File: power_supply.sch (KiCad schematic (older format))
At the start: 0 parts

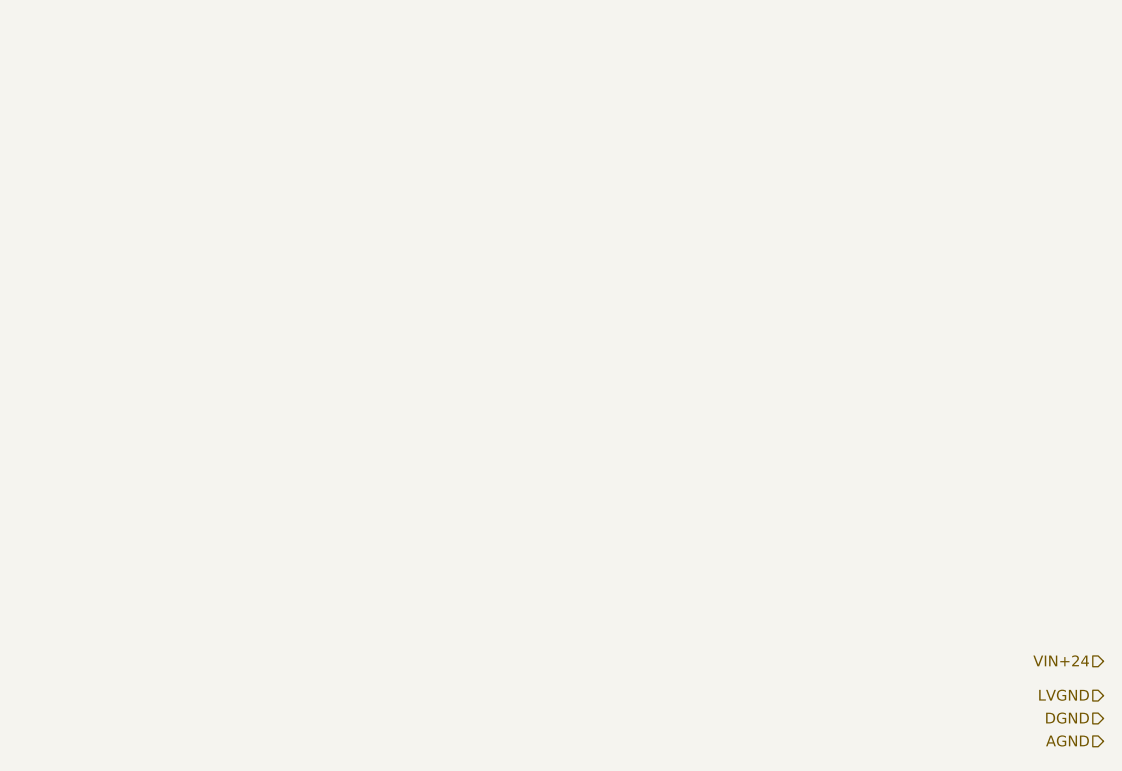
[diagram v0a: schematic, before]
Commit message: added some ICs, started on power, changed sheet sizes
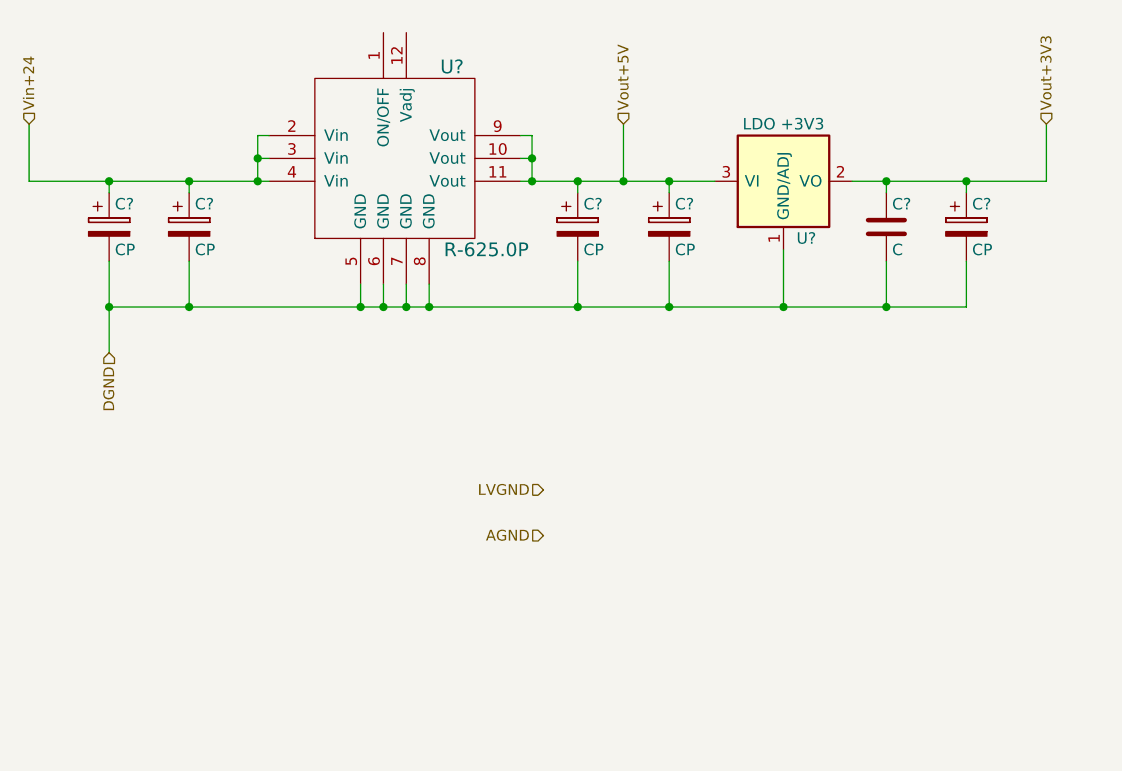
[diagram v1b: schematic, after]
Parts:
- added C? (x5): CP, symbol CP
- added C?: C, symbol C
- added U?: R-625.0P, symbol R-625.0P
- added U?: LDO +3V3, TO_SOT_Packages_SMD:SOT-223, symbol AP1117
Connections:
- net DGND: now also C?.2, C?.2, C?.2, C?.2, C?.2, C?.2, U?.1 (GND/ADJ), U?.5 (GND), U?.6 (GND), U?.7 (GND), U?.8 (GND)
- new net Vin+24: C?.1, C?.1, U?.2 (Vin), U?.3 (Vin), U?.4 (Vin)
- new net Vout+3V3: C?.1, C?.1, U?.2 (VO)
- new net Vout+5V: C?.1, C?.1, U?.10 (Vout), U?.11 (Vout), U?.3 (VI), U?.9 (Vout)
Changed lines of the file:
@@
 EELAYER 25 0
 EELAYER END
-$Descr A4 11693 8268
+$Descr User 7874 5906
 encoding utf-8
 Sheet 10 12
@@
 Comment4 ""
 $EndDescr
-Text HLabel 6050 4700 0    47   Input ~ 0
+Text HLabel 1700 3100 3    47   Input ~ 0
 DGND
-Text HLabel 6050 4800 0    47   Input ~ 0
+Text HLabel 3600 3900 0    47   Input ~ 0
 AGND
-Text HLabel 6050 4450 0    47   Input ~ 0
-VIN+24
-Text HLabel 6050 4600 0    47   Input ~ 0
+Text HLabel 1350 2100 1    47   Input ~ 0
+Vin+24
+Text HLabel 3600 3700 0    47   Input ~ 0
 LVGND
+$Comp
+L CP C?
+U 1 1 572CCDDB
+P 1700 2550
+F 0 "C?" H 1725 2650 50  0000 L CNN
+F 1 "CP" H 1725 2450 50  0000 L CNN
+F 2 "" H 1738 2400 50  0000 C CNN
+F 3 "" H 1700 2550 50  0000 C CNN
+	1    1700 2550
+	1    0    0    -1
+$EndComp
+$Comp
+L CP C?
+U 1 1 572CCE58
+P 2050 2550
+F 0 "C?" H 2075 2650 50  0000 L CNN
+F 1 "CP" H 2075 2450 50  0000 L CNN
+F 2 "" H 2088 2400 50  0000 C CNN
+F 3 "" H 2050 2550 50  0000 C CNN
+	1    2050 2550
+	1    0    0    -1
+$EndComp
+$Comp
+L CP C?
+U 1 1 572CCE73
+P 3750 2550
+F 0 "C?" H 3775 2650 50  0000 L CNN
+F 1 "CP" H 3775 2450 50  0000 L CNN
+F 2 "" H 3788 2400 50  0000 C CNN
+F 3 "" H 3750 2550 50  0000 C CNN
+	1    3750 2550
+	1    0    0    -1
+$EndComp
+$Comp
+L CP C?
+U 1 1 572CCEA6
+P 4150 2550
+F 0 "C?" H 4175 2650 50  0000 L CNN
+F 1 "CP" H 4175 2450 50  0000 L CNN
+F 2 "" H 4188 2400 50  0000 C CNN
+F 3 "" H 4150 2550 50  0000 C CNN
+	1    4150 2550
+	1    0    0    -1
+$EndComp
+$Comp
+L AP1117 U?
+U 1 1 572CD269
+P 4650 2350
+F 0 "U?" H 4750 2100 50  0000 C CNN
+F 1 "LDO +3V3" H 4650 2600 50  0000 C CNN
+F 2 "TO_SOT_Packages_SMD:SOT-223" H 4650 2350 50  0001 C CNN
+F 3 "" H 4650 2350 50  0000 C CNN
+	1    4650 2350
+	1    0    0    -1
+$EndComp
+$Comp
+L CP C?
+U 1 1 572CD599
+P 5450 2550
+F 0 "C?" H 5475 2650 50  0000 L CNN
+F 1 "CP" H 5475 2450 50  0000 L CNN
+F 2 "" H 5488 2400 50  0000 C CNN
+F 3 "" H 5450 2550 50  0000 C CNN
+	1    5450 2550
+	1    0    0    -1
+$EndComp
+$Comp
+L C C?
+U 1 1 572CD71C
+P 5100 2550
+F 0 "C?" H 5125 2650 50  0000 L CNN
+F 1 "C" H 5125 2450 50  0000 L CNN
+F 2 "" H 5138 2400 50  0000 C CNN
+F 3 "" H 5100 2550 50  0000 C CNN
+	1    5100 2550
+	1    0    0    -1
+$EndComp
+Wire Wire Line
+	4950 2350 5800 2350
+Wire Wire Line
+	5800 2350 5800 2100
+Wire Wire Line
+	5450 2400 5450 2350
+Connection ~ 5450 2350
+Wire Wire Line
+	5100 2400 5100 2350
+Connection ~ 5100 2350
+Wire Wire Line
+	3500 2350 4350 2350
+Wire Wire Line
+	3750 2400 3750 2350
+Wire Wire Line
+	4150 2400 4150 2350
+Connection ~ 4150 2350
+Text HLabel 5800 2100 1    47   Input ~ 0
+Vout+3V3
+Connection ~ 3750 2350
+Wire Wire Line
+	3950 2350 3950 2100
+Connection ~ 3950 2350
+Text HLabel 3950 2100 1    47   Input ~ 0
+Vout+5V
+Wire Wire Line
+	1350 2350 1350 2100
+Wire Wire Line
+	1700 2400 1700 2350
+Connection ~ 1700 2350
+Wire Wire Line
+	2050 2400 2050 2350
+Connection ~ 2050 2350
+$Comp
+L R-625.0P U?
+U 1 1 5729C579
+P 2600 2600
+F 0 "U?" H 3200 3350 60  0000 C CNN
+F 1 "R-625.0P" H 3350 2550 60  0000 C CNN
+F 2 "" H 2600 2600 60  0000 C CNN
+F 3 "" H 2600 2600 60  0000 C CNN
+	1    2600 2600
+	1    0    0    -1
+$EndComp
+Wire Wire Line
+	3500 2150 3550 2150
+Wire Wire Line
+	3550 2150 3550 2350
+Connection ~ 3550 2350
+Wire Wire Line
+	3500 2250 3550 2250
+Connection ~ 3550 2250
+Wire Wire Line
+	2400 2350 1350 2350
+Wire Wire Line
+	2400 2250 2350 2250
+Wire Wire Line
+	2350 2150 2350 2350
+Connection ~ 2350 2350
+Wire Wire Line
+	2400 2150 2350 2150
+Connection ~ 2350 2250
+Wire Wire Line
+	5450 2700 5450 2900
+Wire Wire Line
+	5450 2900 1700 2900
+Wire Wire Line
+	1700 2700 1700 3100
+Connection ~ 1700 2900
+Wire Wire Line
+	2800 2800 2800 2900
+Connection ~ 2800 2900
+Wire Wire Line
+	2900 2800 2900 2900
+Connection ~ 2900 2900
+Wire Wire Line
+	3000 2800 3000 2900
+Connection ~ 3000 2900
+Wire Wire Line
+	3100 2800 3100 2900
+Connection ~ 3100 2900
+Wire Wire Line
+	2050 2700 2050 2900
+Connection ~ 2050 2900
+Wire Wire Line
+	4650 2650 4650 2900
+Connection ~ 4650 2900
+Wire Wire Line
+	4150 2700 4150 2900
+Connection ~ 4150 2900
+Wire Wire Line
+	3750 2700 3750 2900
+Connection ~ 3750 2900
+Wire Wire Line
+	5100 2700 5100 2900
+Connection ~ 5100 2900
 $EndSCHEMATC
